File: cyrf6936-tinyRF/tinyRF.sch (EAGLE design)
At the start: 23 parts

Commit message: Added revision and author
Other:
- note added: "Joseph Moreland"
- note added: "v0.1"
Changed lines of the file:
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@@
 Load Capacitance 10pF
 </text>
+<text x="175.26" y="7.62" size="2.1844" layer="97">Joseph Moreland</text>
+<text x="236.22" y="7.62" size="2.1844" layer="97">v0.1</text>
 </plain>
 <instances>

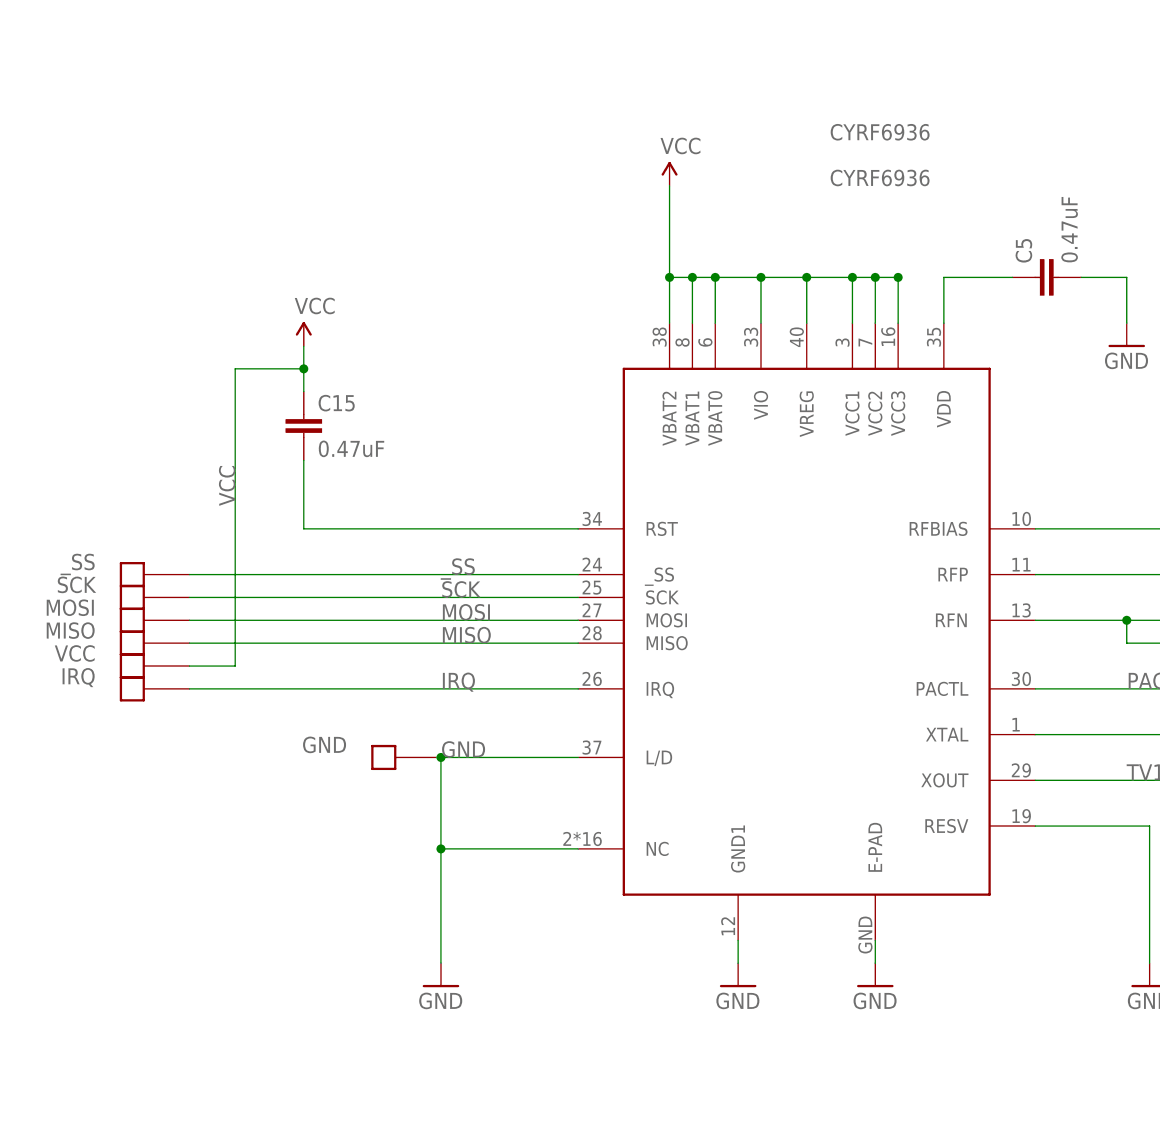
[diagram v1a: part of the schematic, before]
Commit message: Screwed up that last commit.  this update include changes to the production gerber folders.  Adds hackvana to the cyrf6936-BoB and cleans up the fab notes a bit.  Still need to standardize and parameterize the creation of the gerbers.
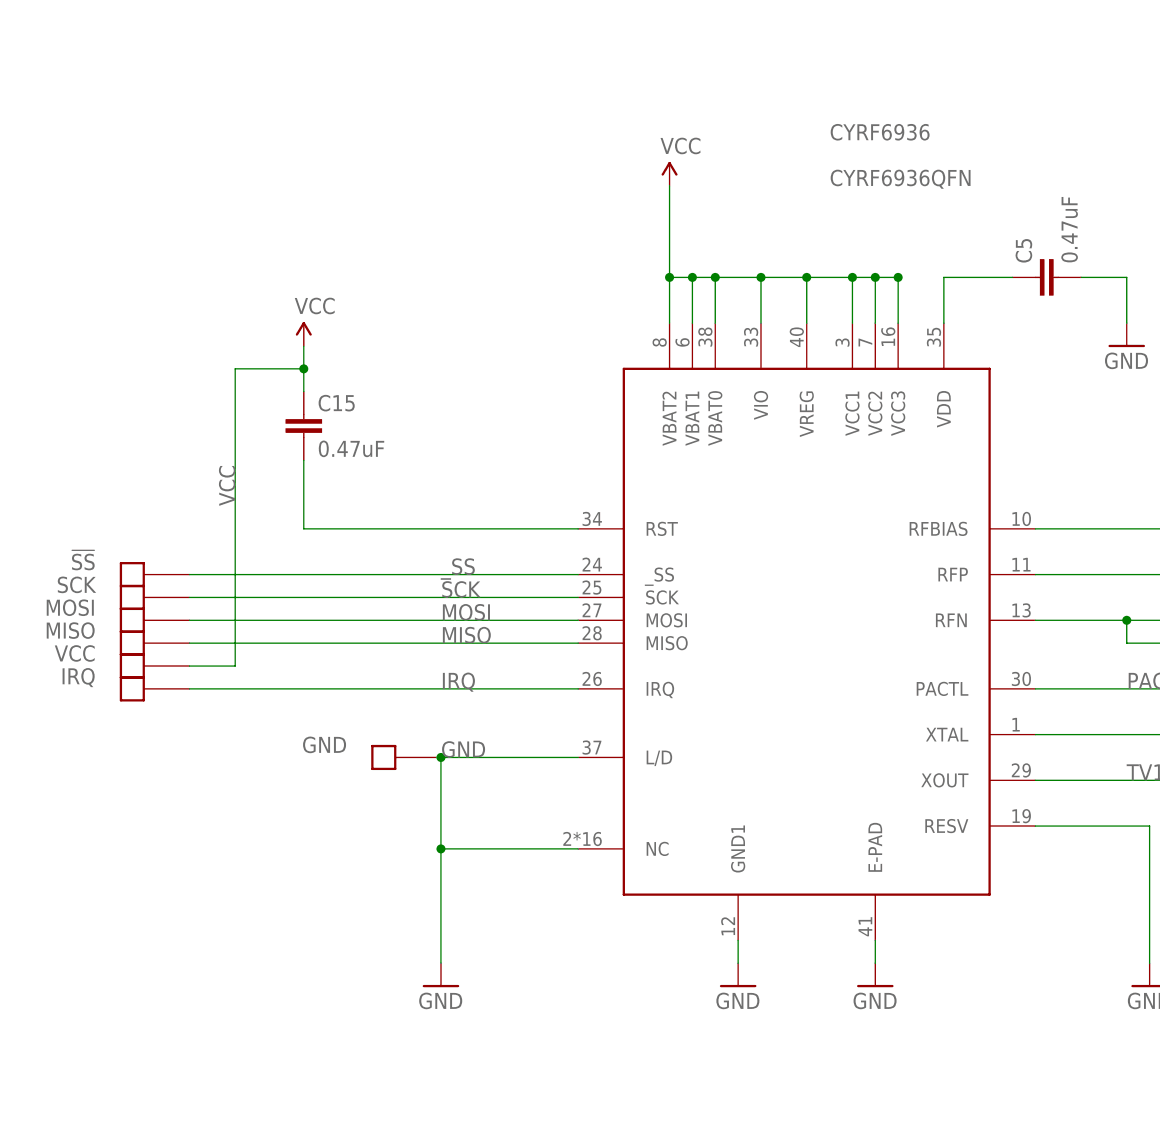
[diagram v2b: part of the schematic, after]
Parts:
- removed _SS: SOLDER_PAD.05X.05, JCM:SOLDER_PAD.05X.05
- added !SS: SOLDER_PADTH, JCM-Connectors:SOLDER_PADTH
- C1, C10, C11, C15, C3, C4, C5, C6, C7, C8, C9: device SparkFun-Passives:CAP0402-CAP -> JCM-Capacitors:CAP0402-CAP
- C14: device SparkFun-Passives:CAP0805 -> JCM-Capacitors:CAP0805
- CYRF6936: value CYRF6936 -> CYRF6936QFN; device JCM:CYRF6936 -> JCM-IC:CYRF6936QFN
- GND, IRQ, MISO, MOSI, SCK, VCC: value SOLDER_PAD.05X.05 -> SOLDER_PADTH; device JCM:SOLDER_PAD.05X.05 -> JCM-Connectors:SOLDER_PADTH
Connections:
- net _SS: now also !SS.NET; no longer _SS.NET
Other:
- moved on the sheet: CYRF6936
